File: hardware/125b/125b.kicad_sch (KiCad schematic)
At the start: 49 parts, among them J1 Guitar in, J2 Barrel_Jack, J3 Conn_02x05_Odd_Even_MountingP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, J4 Guitar out, SW1 SW_Push_SPDT, SW2 RotaryEncoder_Switch, SW3 SW_Push, SW4 SW_Push, U1 L78L05_TO92, U2 TL074

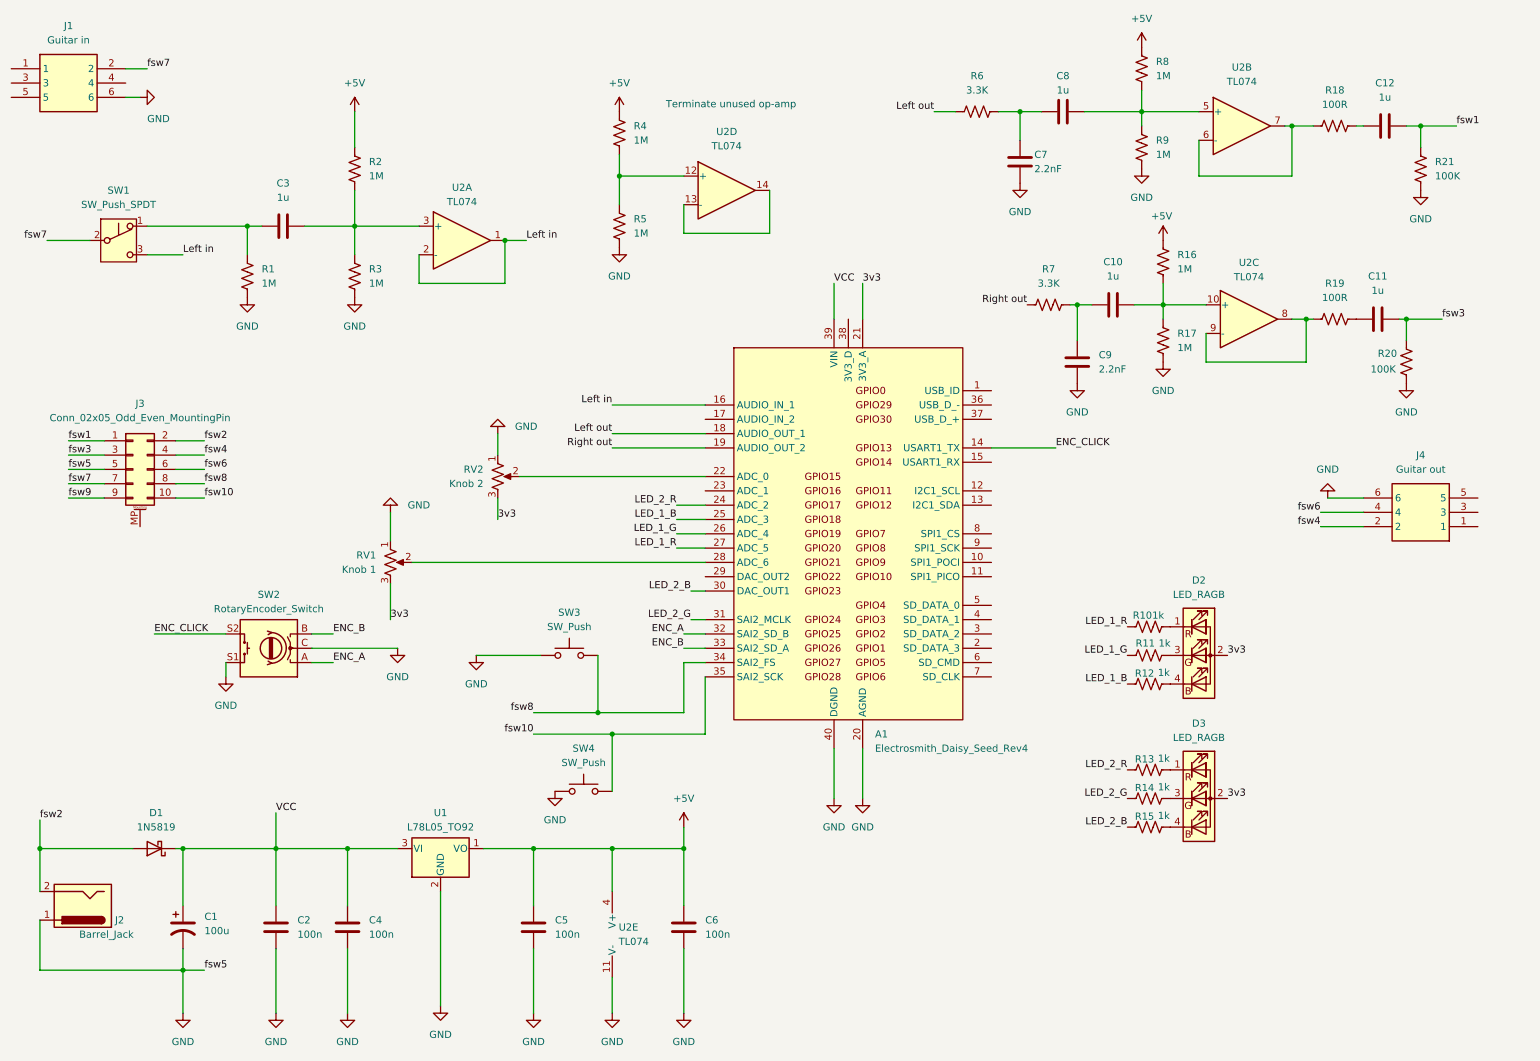
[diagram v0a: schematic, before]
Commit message: Thinner neutrik audio sockets
ALlows power socket to move to back of board again
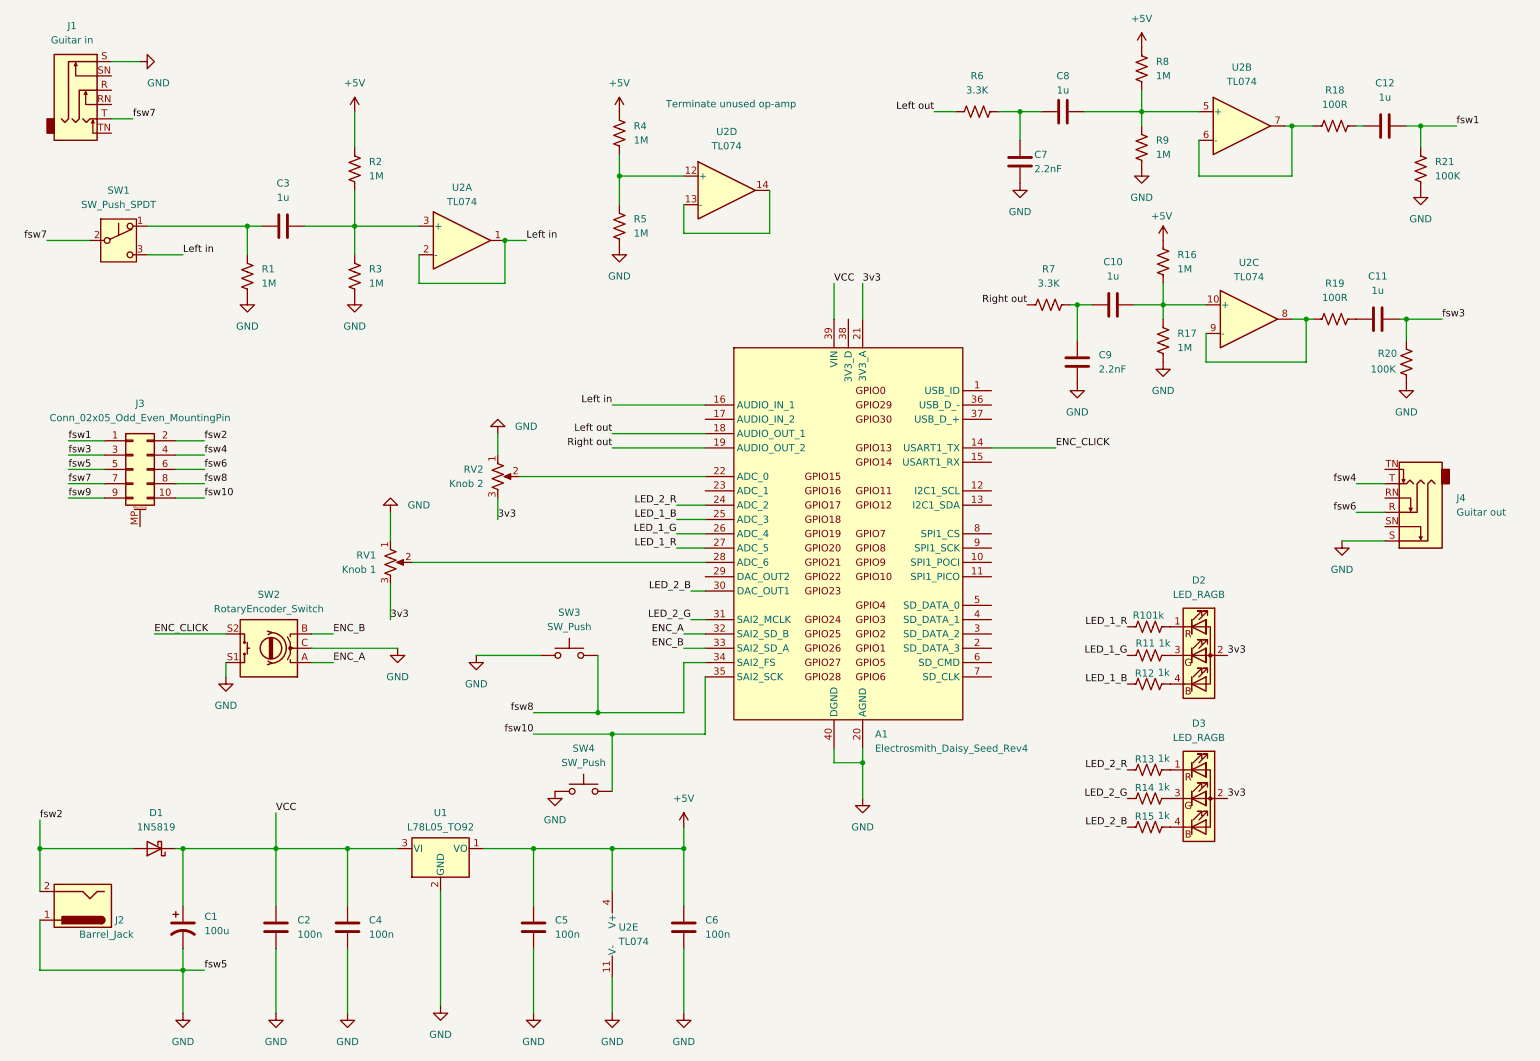
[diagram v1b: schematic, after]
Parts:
- removed J1: Guitar in, Project:NYS215, symbol NYS215:NYS215
- removed J4: Guitar out, Project:NYS215, symbol NYS215:NYS215
- added J1: Guitar in, Project:Jack_6.35mm_Neutrik_NMJ6HCD2_Horizontal, symbol Connector_Audio:NMJ6HCD2
- added J4: Guitar out, Project:Jack_6.35mm_Neutrik_NMJ6HCD2_Horizontal, symbol Connector_Audio:NMJ6HCD2
- SW1: footprint PCM_4ms_Switch:Switch_Toggle_SPDT_SubMini -> Project:mini_switch_jaycar_SPDT
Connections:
- net GND: now also J1.S, J4.S
- net fsw4: now also J4.T
- net fsw6: now also J4.R
- net fsw7: now also J1.T

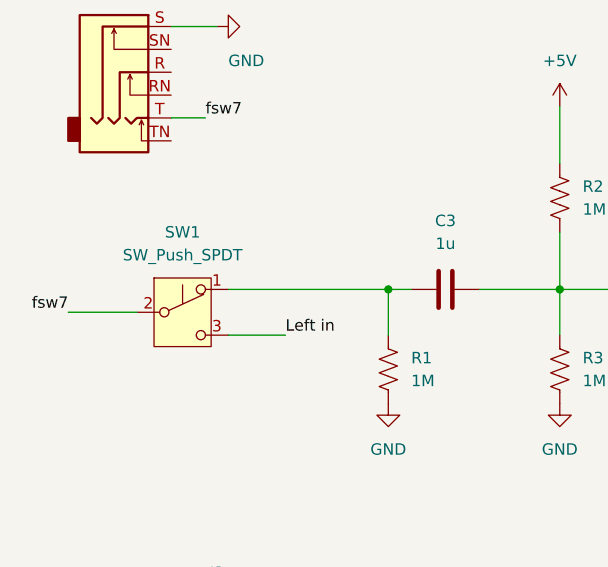
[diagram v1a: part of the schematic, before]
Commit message: Remove line in switch - TL074 is fine
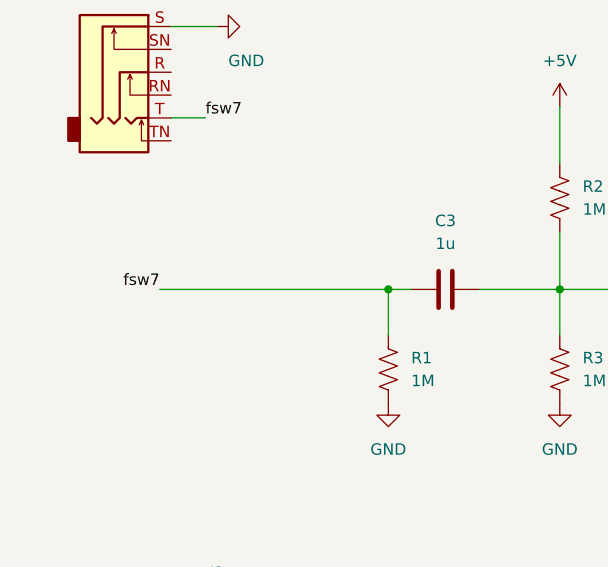
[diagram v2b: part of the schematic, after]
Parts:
- removed SW1: SW_Push_SPDT, Project:mini_switch_jaycar_SPDT, symbol Switch:SW_Push_SPDT
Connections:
- net fsw7: now also C3.1, R1.1
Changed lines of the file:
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@@
 	(wire
 		(pts
-			(xy 38.1 55.88) (xy 44.45 55.88)
-		)
-		(stroke
-			(width 0)
-			(type default)
-		)
-	)
-	(wire
-		(pts
 			(xy 193.04 30.48) (xy 193.04 35.56)
 		)
@@
 	(wire
 		(pts
-			(xy 20.32 53.34) (xy 27.94 53.34)
+			(xy 30.48 50.8) (xy 55.88 50.8)
 		)
 		(stroke
@@
 	(wire
 		(pts
-			(xy 38.1 50.8) (xy 55.88 50.8)
-		)
-		(stroke
-			(width 0)
-			(type default)
-		)
-	)
-	(wire
-		(pts
 			(xy 261.62 33.02) (xy 264.16 33.02)
 		)
@@
 	)
 	(label "fsw7"
-		(at 20.32 53.34 180)
+		(at 30.48 50.8 180)
 		(effects
 			(font
@@
 		)
 	)
-	(label "Left in"
-		(at 44.45 55.88 0)
-		(effects
-			(font
-				(size 1.27 1.27)
-			)
-			(justify left bottom)
-		)
-	)
 	(label "fsw2"
 		(at 19.05 156.21 0)
@@
 					(unit 1)
 				)
-			)
-		)
-	)
-	(symbol
-		(lib_id "Switch:SW_Push_SPDT")
-		(at 33.02 53.34 0)
-		(unit 1)
-		(exclude_from_sim no)
-		(in_bom yes)
-		(on_board yes)
-		(dnp no)
-		(fields_autoplaced yes)
-		(property "Reference" "SW1"
-			(at 33.02 44.45 0)
-			(effects
-				(font
-					(size 1.27 1.27)
-				)
-			)
-		)
-		(property "Value" "SW_Push_SPDT"
-			(at 33.02 46.99 0)
-			(effects
-				(font
-					(size 1.27 1.27)
-				)
-			)
-		)
-		(property "Footprint" "Project:mini_switch_jaycar_SPDT"
-			(at 33.02 53.34 0)
-			(effects
-				(font
-					(size 1.27 1.27)
-				)
-				(hide yes)
-			)
-		)
-		(property "Datasheet" "~"
-			(at 33.02 53.34 0)
-			(effects
-				(font
-					(size 1.27 1.27)
-				)
-				(hide yes)
-			)
-		)
-		(property "Description" "Momentary Switch, single pole double throw"
-			(at 33.02 53.34 0)
-			(effects
-				(font
-					(size 1.27 1.27)
-				)
-				(hide yes)
-			)
-		)
-		(pin "3"
-		)
-		(pin "2"
-		)
-		(pin "1"
-		)
-		(instances
-			(project ""
-				(path "/12e895f7-e5ae-4934-aed6-e6e04c63dd03"
-					(reference "SW1")
-					(unit 1)
-				)
